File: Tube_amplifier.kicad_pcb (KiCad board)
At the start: 2 copper layers, 140 x 54 mm, 23 parts, among them J2 Input, J3 Power, J4 Output, T1 Transformer_SP_1S, U1 6N2P, U2 6P14P

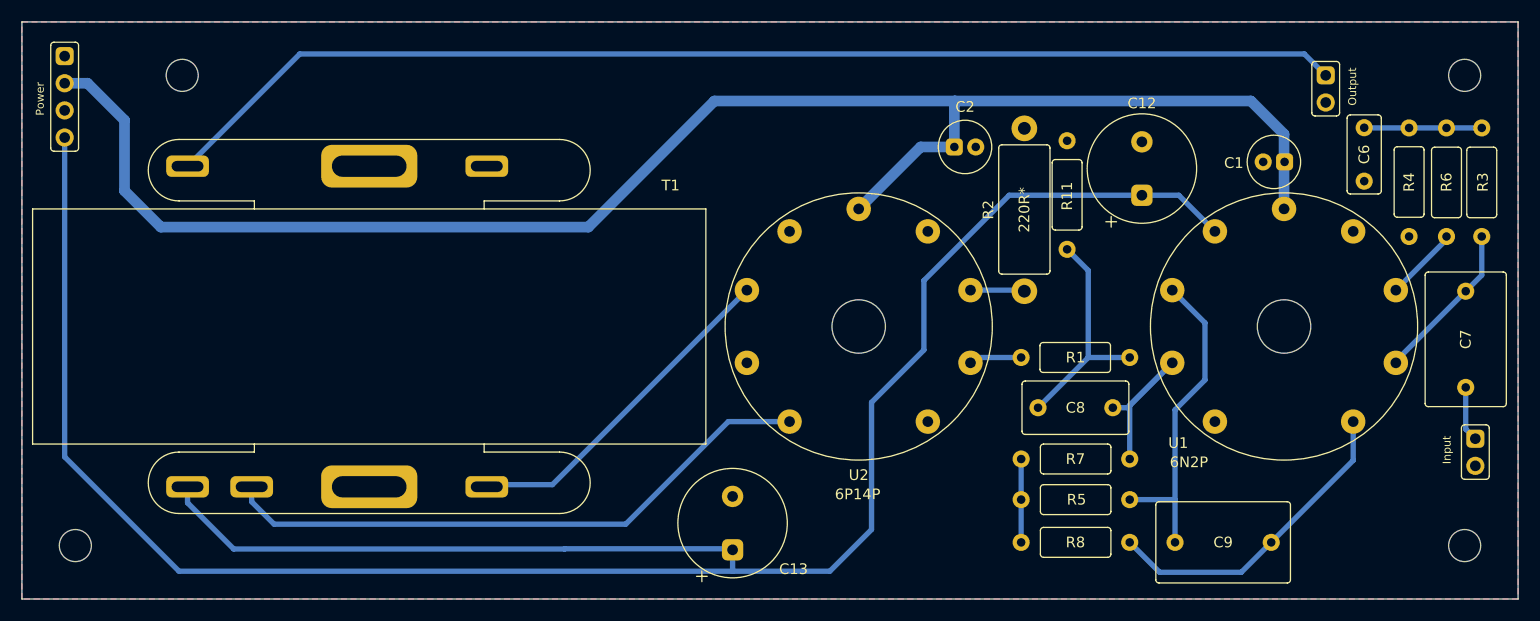
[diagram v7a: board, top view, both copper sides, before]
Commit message: Curved traces
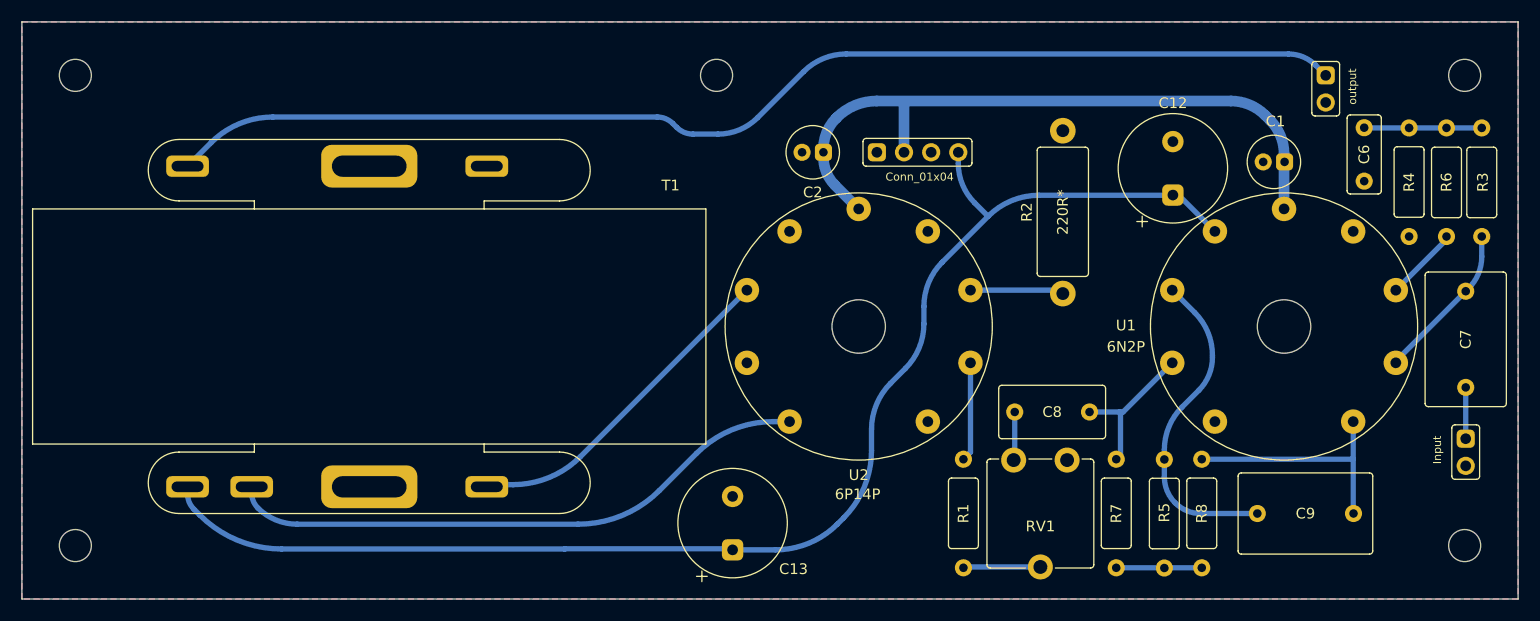
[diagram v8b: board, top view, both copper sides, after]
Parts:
- removed R11: 100k, spdf1626_lib:R_THT_025W
- added RV1: 100k, spdf1626_lib:Potentiometer_THT_CA9V, F.Cu at (142.8, 117.0)
- J3: value Power -> Conn_01x04
- J4: value Output -> output
- moved J3 76.5 mm to (130.0, 88.2), turned to 90 degrees
- moved R1 25.1 mm to (138.1, 127.1), turned to 90 degrees
- moved R8 17.1 mm to (160.4, 127.1), turned to 90 degrees
- moved R5 14.8 mm to (156.9, 127.1), turned to 90 degrees
- moved R7 13.5 mm to (152.4, 127.1), turned to 90 degrees
- moved C2 12.3 mm to (125.0, 88.2), turned to 180 degrees
- moved C9 8.16 mm to (170.1, 122.0)
- moved R2 3.61 mm to (147.4, 101.4)
- moved C12 2.90 mm to (157.7, 92.2)
- moved C8 2.22 mm to (146.4, 112.5)
- moved J2 0.90 mm to (185.1, 115.0)
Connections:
- R1 pad 1: Net-(C8-Pad2) -> Net-(R1-Pad1)
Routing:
- net 240V: track 225.0 -> 127.5 mm
- net +6V: track 152.4 -> 64.9 mm
- net Net-(C8-Pad2): track 21.5 -> 4.54 mm
- net Net-(C9-Pad2): track 30.0 -> 22.7 mm
- net Net-(R1-Pad1): track 0.00 -> 7.23 mm
- net Net-(R1-Pad2): track 4.95 -> 9.29 mm
- net Net-(C8-Pad1): track 18.5 -> 14.3 mm
- net Net-(R2-Pad1): track 5.08 -> 8.77 mm
- net Net-(T1-Pad2): track 56.6 -> 55.2 mm
- net Net-(C9-Pad1): track 30.3 -> 30.8 mm
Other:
- outline, holes or cut-outs redrawn
